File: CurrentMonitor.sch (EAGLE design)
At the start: 21 parts, among them IC1 MEGA8-AI, IC2 INA138, IC3 INA138, J1 AVR_SPI_PRG_6OFFSET_PADS, Q1 10MHz, X1 MSTBV4, X2 MSTBV4, X3 MSTBV2

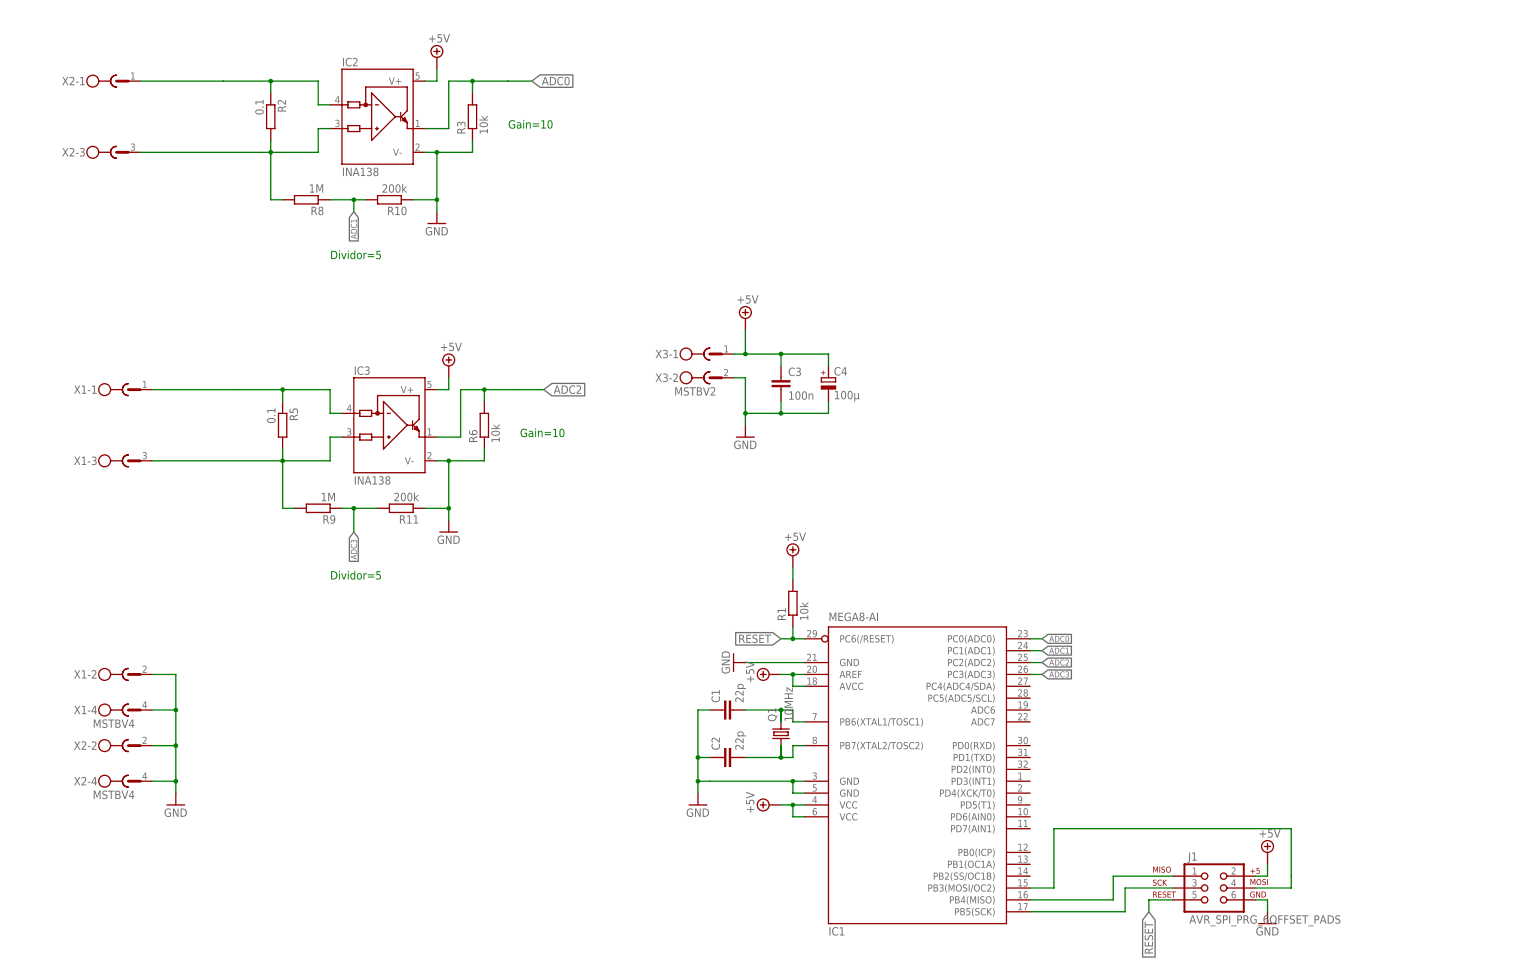
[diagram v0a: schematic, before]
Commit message: Redesign first part, more to follow.
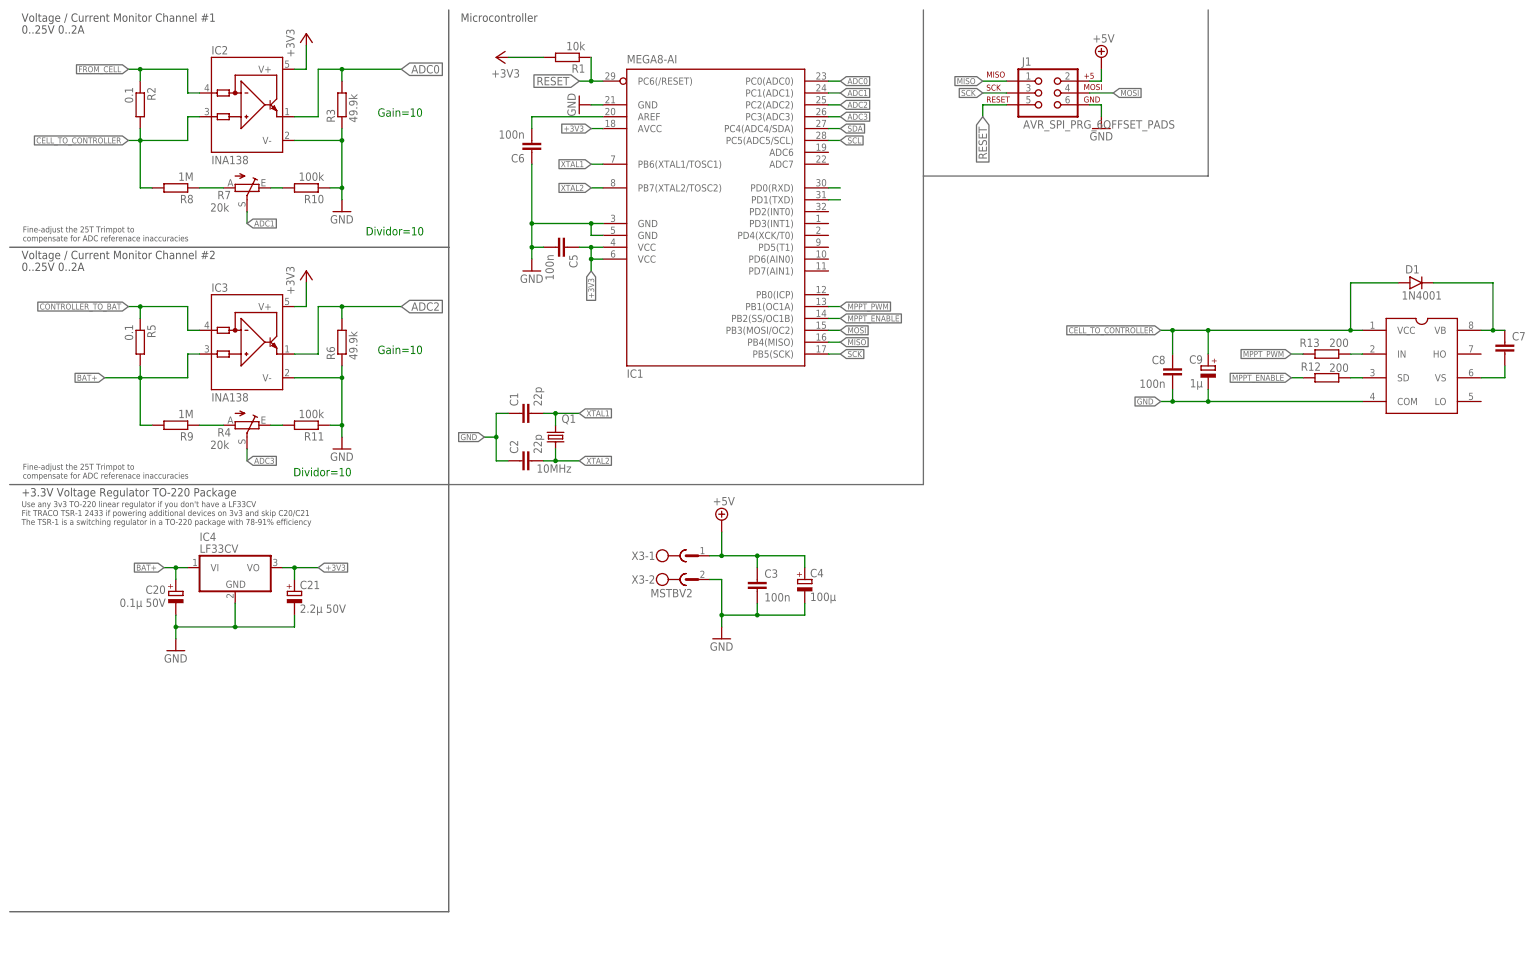
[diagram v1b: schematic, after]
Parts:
- removed X1, X2: MSTBV4, con-phoenix-508:MSTBV4
- added C20: 0.1µ 50V, rcl:CPOL-EUA/3216-18R
- added C21: 2.2µ 50V, rcl:CPOL-EUB
- added C5, C6, C8: 100n, resistor:C-EUC0805
- added C7: (no value), resistor:C-EUC0805
- added C9: 1µ, rcl:CPOL-EUA
- added D1: 1N4001, gm-diodes:DO41.3
- added IC4: LF33CV, linear:7805TV
- added R12, R13: 200, rcl:R-EU_R1206
- added R4, R7: 20k, pot:TRIM_EU-S64W
- added U$1: IR2104S, ir-2104:IR2104S
- R10, R11: value 200k -> 100k; device rcl:R-EU_0207/10 -> rcl:R-EU_R1206
- R3, R6: value 10k -> 49.9k; device rcl:R-EU_0207/10 -> rcl:R-EU_R1206
- R8, R9: device rcl:R-EU_0207/10 -> rcl:R-EU_R1206
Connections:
- net N$1 renamed XTAL2
- net N$2 renamed XTAL1
- net N$6 renamed MISO
- net N$7 renamed SCK
- net N$8 renamed MOSI
- removed net +5V: C3.1, C4.+, IC1.AREF, IC1.AVCC, IC1.VCC@1, IC1.VCC@2, IC2.V+, IC3.V+, J1.2, R1.2, X3-1.1
- new net +3V3: C21.+, C3.1, C4.+, C5.1, IC1.AVCC, IC1.VCC@1, IC1.VCC@2, IC2.V+, IC3.V+, J1.2, R1.2, X3-1.1
- new net BAT+: C20.+, IC3.IN+, IC4.VI, R5.2, R9.2
- new net CELL_TO_CONTROLLER: C8.1, C9.+, D1.A, IC2.IN+, R2.2, R8.2, U$1.VCC
- new net CONTROLLER_TO_BAT: IC3.IN-, R5.1
- new net FROM_CELL: IC2.IN-, R2.1
- new net MPPT_ENABLE: IC1.PB2(SS/OC1B), R12.1
- new net MPPT_PWM: IC1.PB1(OC1A), R13.1
- new net N$1: C6.2, IC1.AREF
- new net N$11: C7.2, U$1.VS
- new net N$2: R11.2, R4.E
- new net N$3: R10.2, R7.E
- new net N$6: IC1.PD0(RXD)
- new net N$7: IC1.PD1(TXD)
- new net N$8: R12.2, U$1.SD
- new net SCL: IC1.PC5(ADC5/SCL)
- new net SDA: IC1.PC4(ADC4/SDA)
- net ADC1: now also R7.S; no longer R10.2, R8.1
- net ADC3: now also R4.S; no longer R11.2, R9.1
- net GND: now also C20.-, C21.-, C5.2, C6.1, C8.2, C9.-, IC4.GND, U$1.COM; no longer X1-2.1, X1-4.1, X2-2.1, X2-4.1
- net N$10: now also R13.2, U$1.IN; no longer IC3.IN-, R5.1, X1-1.1
- net N$4: now also R7.A, R8.1; no longer IC2.IN+, R2.2, R8.2, X2-3.1
- net N$5: now also R4.A, R9.1; no longer IC2.IN-, R2.1, X2-1.1
- net N$9: now also C7.1, D1.C, U$1.VB; no longer IC3.IN+, R5.2, R9.2, X1-3.1
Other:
- note added: "+3.3V Voltage Regulator TO-220 Package"
- note added: "0..25V 0..2A"
- note added: "Dividor=10"
- note added: "Fine-adjust the 25T Trimpot to compensate for ADC referenace inaccuracies"
- note added: "Microcontroller"
- note added: "Use any 3v3 TO-220 linear regulator if you don't have a LF33CV Fit TRACO TSR-1 2433 if powering additional devices on 3v3 and skip C20/C21 The TSR-1 is a switching regulator in a TO-220 package with 78-91% efficiency"
- note added: "Voltage / Current Monitor Channel #1"
- note added: "Voltage / Current Monitor Channel #2"
- note removed: "Dividor=5"
- moved on the sheet: C1, C2, C3, C4, IC1, IC2, IC3, J1, Q1, R1, R10, R11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

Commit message: More updates
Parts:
- removed C3: 100n, rcl:C-EUC0805
- removed C4: 100µ, rcl:CPOL-EUD
- removed X3: MSTBV2, con-phoenix-508:MSTBV2
- added C10: 100n, resistor:C-EUC0805
- added C11, C12: 100µ, rcl:CPOL-EUF
- added C13, C14: 1µ, rcl:CPOL-EUB
- added D2: 1N4001, gm-diodes:DO41.3
- added D3: UF4007, diode:1N4004
- added L1: 33µ, Inductor-Fastron:L-EUPISM
- added Q2, Q3, Q4, Q5, Q6: IRLZ34N, transistor-power:IRF520
- added R14: 470k, resistor:R-EU_R1206
- added R15, R16: 5, resistor:R-EU_R1206
- added R17: 200, resistor:R-EU_R1206
- added R18, R19: 100k, rcl:R-EU_R1206
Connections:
- net N$6 renamed RXD
- net N$7 renamed TXD
- new net EN_3V3: Q5.G, R18.1
- new net EN_CIRCUIT: Q6.G, R19.1
- new net GND_3V3: Q5.D
- new net GND_CIRCUIT: Q6.D
- new net HO: R15.1, U$1.HO
- new net LO: R16.1, U$1.LO
- new net N$12: D2.C, Q2.G, R14.1
- new net N$13: D2.A, Q3.G, R15.2
- new net N$14: Q2.D, Q3.D
- new net N$17: C10.1, R17.1
- new net VS: C7.2, Q3.S, Q4.D, U$1.VS
- net +3V3: now also IC4.VO; no longer C3.1, C4.+, X3-1.1
- net CELL_TO_CONTROLLER: now also C12.+, C14.+, Q2.S, R14.2
- net CONTROLLER_TO_BAT: now also C11.+, C13.+, L1.2, R17.2
- net GND: now also C10.2, C11.-, C12.-, C13.-, C14.-, D3.A, D3.C, L1.1, Q4.S, Q5.S, Q6.S, R18.2, R19.2; no longer C3.2, C4.-, X3-2.1
- net N$11: now also Q4.G, R16.2; no longer C7.2, U$1.VS
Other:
- note added: "3.3V and main output switching"
- note added: "MOSFET Driver Circuit"
- note added: "Step Down Circuit"
- moved on the sheet: C7, C8, C9, D1, R12, R13

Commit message: Bleh.
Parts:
- added C3: 0.1µ, rcl:CPOL-EUB
- added C4: 0.33µ, rcl:CPOL-EUB
- added IC5: 78L05SMD, linear:78L05SMD
- added Q7, Q8: IRF9530, transistor-power:IRF9530
- added R20, R21: 10k, rcl:R-EU_R1206
- added X1, X2, X3, X4: MSTBV2, con-phoenix-508:MSTBV2
- added X6, X7: MSTBV3, con-phoenix-508:MSTBV3
- R2, R5: device rcl:R-EU_0207/10 -> resistor:R-EU_R1206
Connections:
- new net +5V: C3.+, IC5G$1.VOUT
- new net N$15: IC1.PD6(AIN0)
- new net N$16: IC1.PD5(T1)
- new net N$18: IC1.PD4(XCK/T0)
- new net N$19: IC1.PD3(INT1)
- new net N$6: IC1.PB0(ICP)
- new net N$7: IC1.PD7(AIN1)
- net +3V3: now also R20.1, R21.1, X4-1.1
- net BAT+: now also C4.+, IC5G$1.VIN, X2-1.1, X3-1.1
- net FROM_CELL: now also X1-1.1
- net GND: now also C3.-, C4.-, IC5G$1.GND@1, IC5G$1.GND@2, IC5G$1.GND@3, IC5G$1.GND@4, X1-2.1, X2-2.1
- net GND_3V3: now also X4-2.1
- net GND_CIRCUIT: now also X3-2.1
- net SCL: now also R21.2
- net SDA: now also R20.2
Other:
- note added: "+5V 100mA"
- note added: "Ersetzen durch P-channel + driver"
- note added: "ISP"
- note added: "I²C Pullups"

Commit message: Added initial board
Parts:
- removed C3: 0.1µ, rcl:CPOL-EUB
- removed C4: 0.33µ, rcl:CPOL-EUB
- removed IC5: 78L05SMD, linear:78L05SMD
- removed R18: 100k, rcl:R-EU_R1206
- removed X4: MSTBV2, con-phoenix-508:MSTBV2
- removed X6, X7: MSTBV3, con-phoenix-508:MSTBV3
- added D4, D5: BAV203, semicon-smd-ipc:D-SOD-80
- added JP1: (no value), pinhead:PINHD-1X6
- added JP2: (no value), pinhead:PINHD-1X4
- added Q9: BC847, transistor-npn:BC847ALT1SMD
- added R22, R23, R24: 10k, rcl:R-EU_R1206
- added X5: MSTBV2, con-phoenix-508:MSTBV2
- Q5: value IRLZ34N -> (none); device transistor-power:IRF520 -> crystal:CRYSTALHC49S
- Q6: value IRLZ34N -> BC847; device transistor-power:IRF520 -> transistor-npn:BC847ALT1SMD
- R19: value 100k -> 10k
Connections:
- removed net +5V: C3.+, IC5G$1.VOUT
- removed net GND_3V3: Q5.D, X4-2.1
- removed net GND_CIRCUIT: Q6.D, X3-2.1
- removed net N$6: IC1.PB0(ICP)
- removed net N$7: IC1.PD7(AIN1)
- new net N$20: Q6.C, Q8.G, R19.2
- new net N$21: Q6.B, R22.2
- new net N$22: Q7.G, Q9.C, R23.2
- new net N$23: Q9.B, R24.2
- new net N$24: D4.C, Q8.D, X3-1.1
- new net N$25: D5.C, Q7.D, X5-1.1
- net +3V3: now also JP1.3, JP1.4, Q7.S, R23.1; no longer J1.2, X4-1.1
- net BAT+: now also JP1.5, JP1.6, Q8.S, R19.1; no longer C4.+, IC5G$1.VIN, X3-1.1
- net EN_3V3: now also IC1.PB0(ICP), R24.1; no longer Q5.G, R18.1
- net EN_CIRCUIT: now also IC1.PD7(AIN1), R22.1; no longer Q6.G, R19.1
- net GND: now also D4.A, D5.A, JP1.1, JP1.2, Q6.E, Q9.E, X3-2.1, X5-2.1; no longer C10.2, C3.-, C4.-, D3.C, IC5G$1.GND@1, IC5G$1.GND@2, IC5G$1.GND@3, IC5G$1.GND@4, L1.1, Q5.S, Q6.S, R18.2, R19.2
- net RXD: now also JP2.3
- net SCL: now also JP2.2
- net SDA: now also JP2.1
- net TXD: now also JP2.4
- net VS: now also C10.2, D3.C, L1.1
- net XTAL1: now also Q5.2
- net XTAL2: now also Q5.1
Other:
- note added: "3V3 Output Switching"
- note added: "Circuit Output Switching"
- note removed: "+5V 100mA"
- note removed: "3.3V and main output switching"
- note removed: "Ersetzen durch P-channel + driver"
- moved on the sheet: Q7, Q8, R19, X1-1, X1-2, X2-1, X2-2, X3-1, X3-2

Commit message: Second revision, dual layer
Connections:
- net MPPT_ENABLE: now also IC1.PB1(OC1A); no longer IC1.PB2(SS/OC1B)
- net MPPT_PWM: now also IC1.PB2(SS/OC1B); no longer IC1.PB1(OC1A)
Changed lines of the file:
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@@
 <net name="MPPT_PWM" class="0">
+<segment>
+<pinref part="R13" gate="G$1" pin="1"/>
+<wire x1="320.04" y1="205.74" x2="317.5" y2="205.74" width="0.1524" layer="91"/>
+<label x="317.5" y="205.74" size="1.27" layer="97" rot="R180" xref="yes"/>
+</segment>
+<segment>
+<pinref part="IC1" gate="G$1" pin="PB2(SS/OC1B)"/>
+<wire x1="175.26" y1="198.12" x2="177.8" y2="198.12" width="0.1524" layer="91"/>
+<label x="177.8" y="198.12" size="1.27" layer="97" xref="yes"/>
+</segment>
+</net>
+<net name="MPPT_ENABLE" class="0">
+<segment>
+<pinref part="R12" gate="G$1" pin="1"/>
+<wire x1="320.04" y1="200.66" x2="317.5" y2="200.66" width="0.1524" layer="91"/>
+<label x="317.5" y="200.66" size="1.27" layer="97" rot="R180" xref="yes"/>
+</segment>
 <segment>
 <pinref part="IC1" gate="G$1" pin="PB1(OC1A)"/>
@@
 <label x="177.8" y="200.66" size="1.27" layer="97" xref="yes"/>
 </segment>
-<segment>
-<pinref part="R13" gate="G$1" pin="1"/>
-<wire x1="320.04" y1="205.74" x2="317.5" y2="205.74" width="0.1524" layer="91"/>
-<label x="317.5" y="205.74" size="1.27" layer="97" rot="R180" xref="yes"/>
-</segment>
 </net>
-<net name="MPPT_ENABLE" class="0">
-<segment>
-<pinref part="IC1" gate="G$1" pin="PB2(SS/OC1B)"/>
-<wire x1="175.26" y1="198.12" x2="177.8" y2="198.12" width="0.1524" layer="91"/>
-<label x="177.8" y="198.12" size="1.27" layer="97" xref="yes"/>
-</segment>
-<segment>
-<pinref part="R12" gate="G$1" pin="1"/>
-<wire x1="320.04" y1="200.66" x2="317.5" y2="200.66" width="0.1524" layer="91"/>
-<label x="317.5" y="200.66" size="1.27" layer="97" rot="R180" xref="yes"/>
-</segment>
-</net>

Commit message: Added slightly larger traces and adjusted some components in order to support currents up to 10A
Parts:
- added F1: (no value), fuse:SHKOG
- added L2: 10µ, Inductor-Fastron:L-EUPISR
- R4, R7: device pot:TRIM_EU-S64W -> rcl:R-TRIMM64P
- X1, X2, X3, X5: value MSTBV2 -> MSTBA2; device con-phoenix-508:MSTBV2 -> con-phoenix-508:MSTBA2
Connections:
- new net N$123: F1.2A, IC2.IN-, R2.1
- net CONTROLLER_TO_BAT: now also L2.1
- net FROM_CELL: now also F1.1A; no longer IC2.IN-, R2.1
- net VS: now also L2.2
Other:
- note added: "Fit either L1 or L2, depending on if you're using 2A or 10A max."
- moved on the sheet: C11, C13, D3

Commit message: Added heatsink + LEDs
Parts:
- removed F1: (no value), fuse:SHKOG
- added LED1, LED2, LED3, LED4, LED5: (no value), led:LEDCHIPLED_1206
- added R18, R25, R26, R27, R28: (no value), rcl:R-EU_R1206
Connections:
- removed net N$123: F1.2A, IC2.IN-, R2.1
- removed net N$15: IC1.PD6(AIN0)
- removed net N$16 (its old number): IC1.PD5(T1)
- removed net N$19: IC1.PD3(INT1)
- new net LED1: IC1.PD2(INT0), LED1.A
- new net LED2: IC1.PD3(INT1), LED2.A
- new net LED3: IC1.PD4(XCK/T0), LED3.A
- new net LED4: IC1.PD5(T1), LED4.A
- new net LED5: IC1.PD6(AIN0), LED5.A
- new net N$26: LED3.C, R26.1
- new net N$29: LED4.C, R27.1
- new net N$32: LED5.C, R28.1
- new net N$6: LED1.C, R18.1
- net FROM_CELL: now also IC2.IN-, R2.1; no longer F1.1A
- net GND: now also R18.2, R25.2, R26.2, R27.2, R28.2
- net N$18: now also LED2.C, R25.1; no longer IC1.PD4(XCK/T0)
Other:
- moved on the sheet: X3-1, X3-2
